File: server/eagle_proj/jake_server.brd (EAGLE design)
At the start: 66.8 x 80.5 mm, 16 parts, among them IC1 7805DT

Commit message: Fix voltage regulator
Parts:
- removed IC1: 7805DT, linear:TO252
- added C1: 100uf, SparkFun-Capacitors:1206
- added IC2: REG1117, burr-brown:SOT223
- moved C8 6.21 mm to (40.2, 47.2), turned to 180 degrees
- moved R1 1.35 mm to (10.5, 78.0)
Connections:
- net GND: now also C1.1, IC2.1; no longer IC1.3
- net N$1: now also C1.2, IC2.3; no longer IC1.1
- net VCC: now also IC2.2; no longer IC1.2
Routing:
- net GND: track 276.0 -> 251.2 mm
- net VCC: track 144.6 -> 127.9 mm
- net N$1: track 48.1 -> 60.4 mm, vias 2 -> 3
- net N$21: track 79.9 -> 79.2 mm

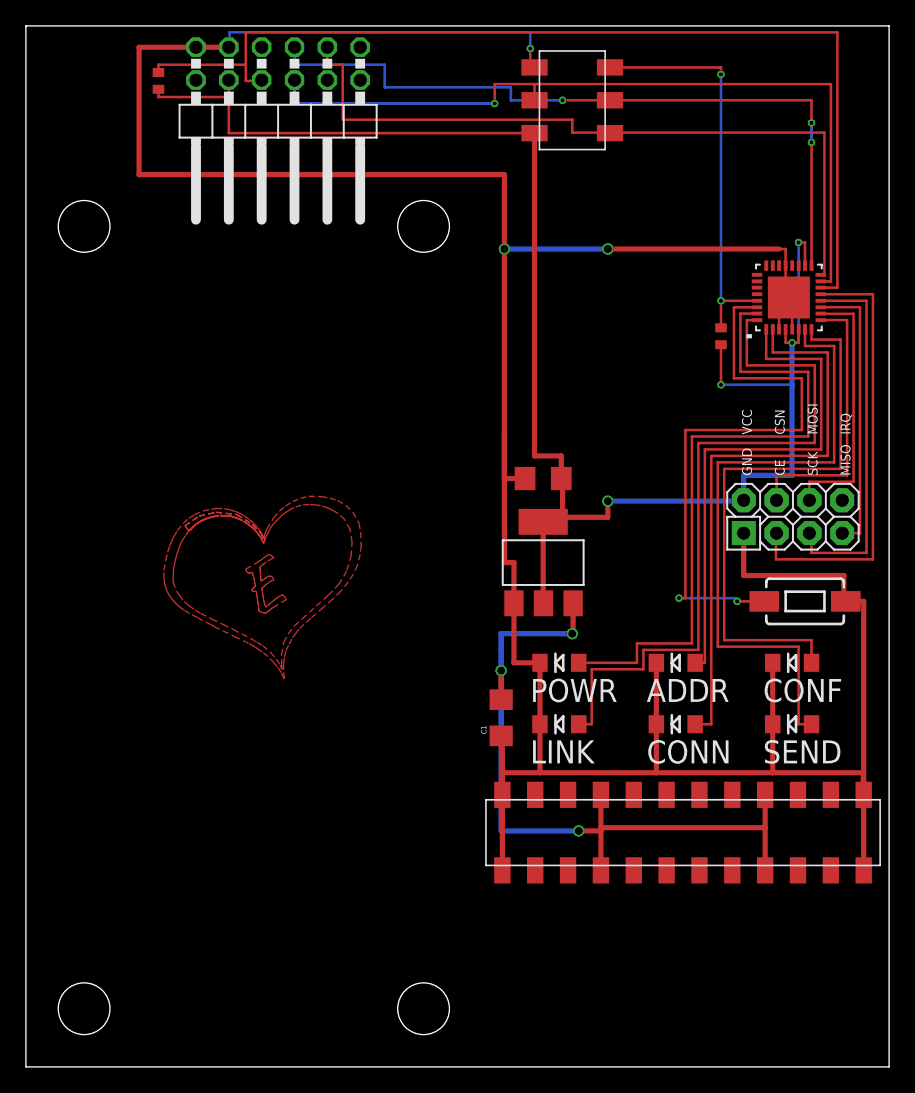
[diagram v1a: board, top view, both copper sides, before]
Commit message: server bill of materials
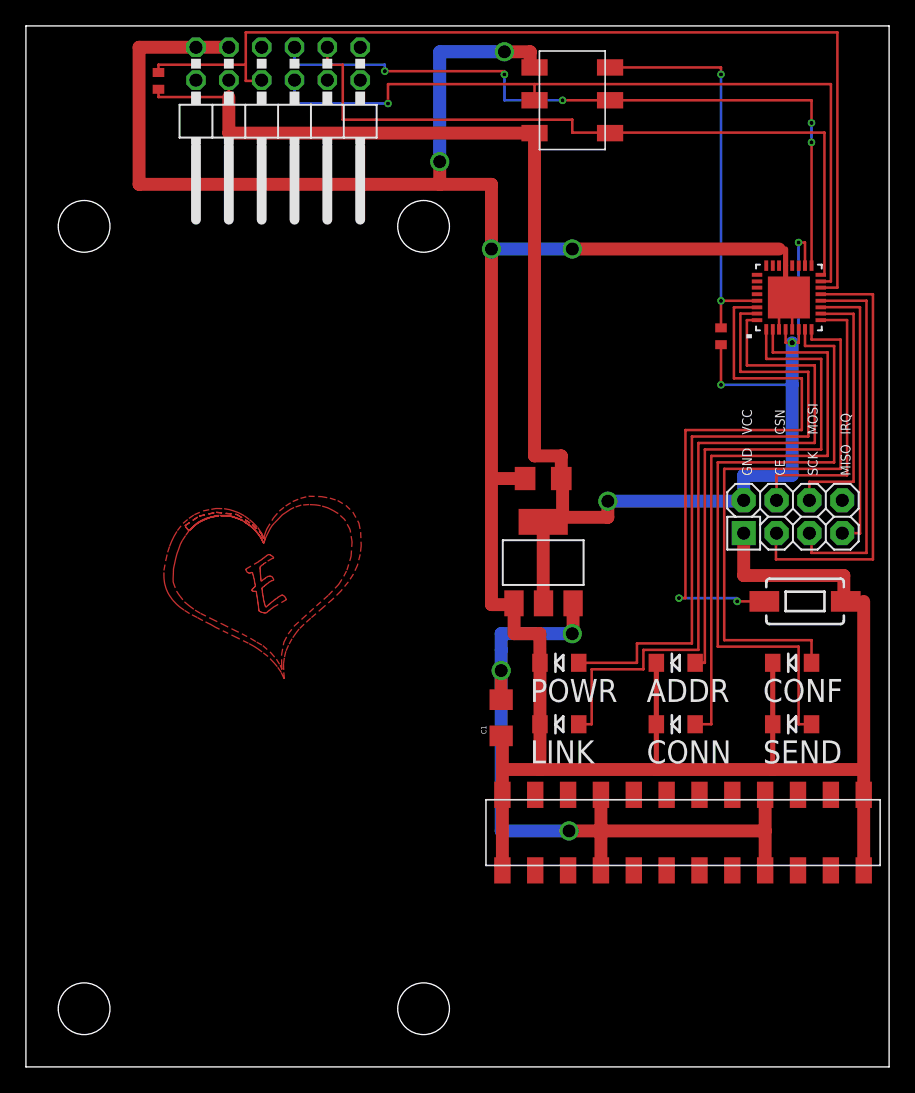
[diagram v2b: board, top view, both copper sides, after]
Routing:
- net GND: track 251.2 -> 240.8 mm, vias 3 -> 4
- net N$11: vias 3 -> 5
